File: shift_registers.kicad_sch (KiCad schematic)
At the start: 2 parts

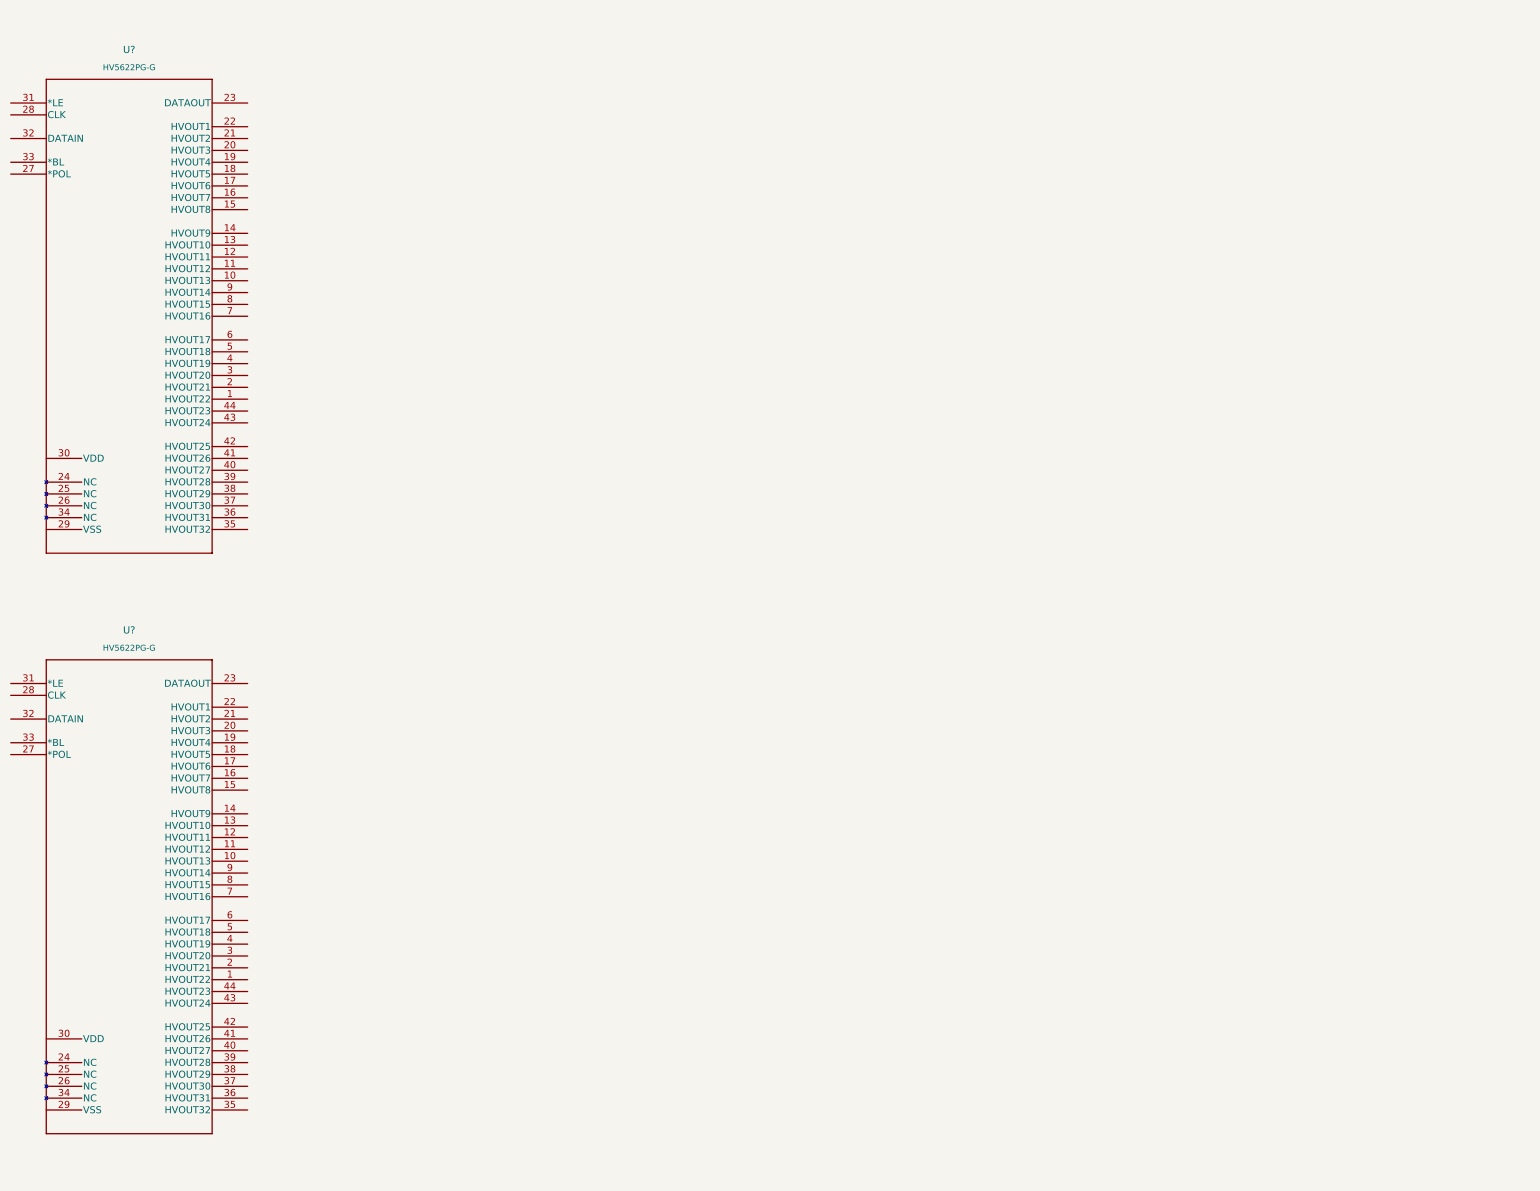
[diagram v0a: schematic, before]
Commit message: added a nixie symbol
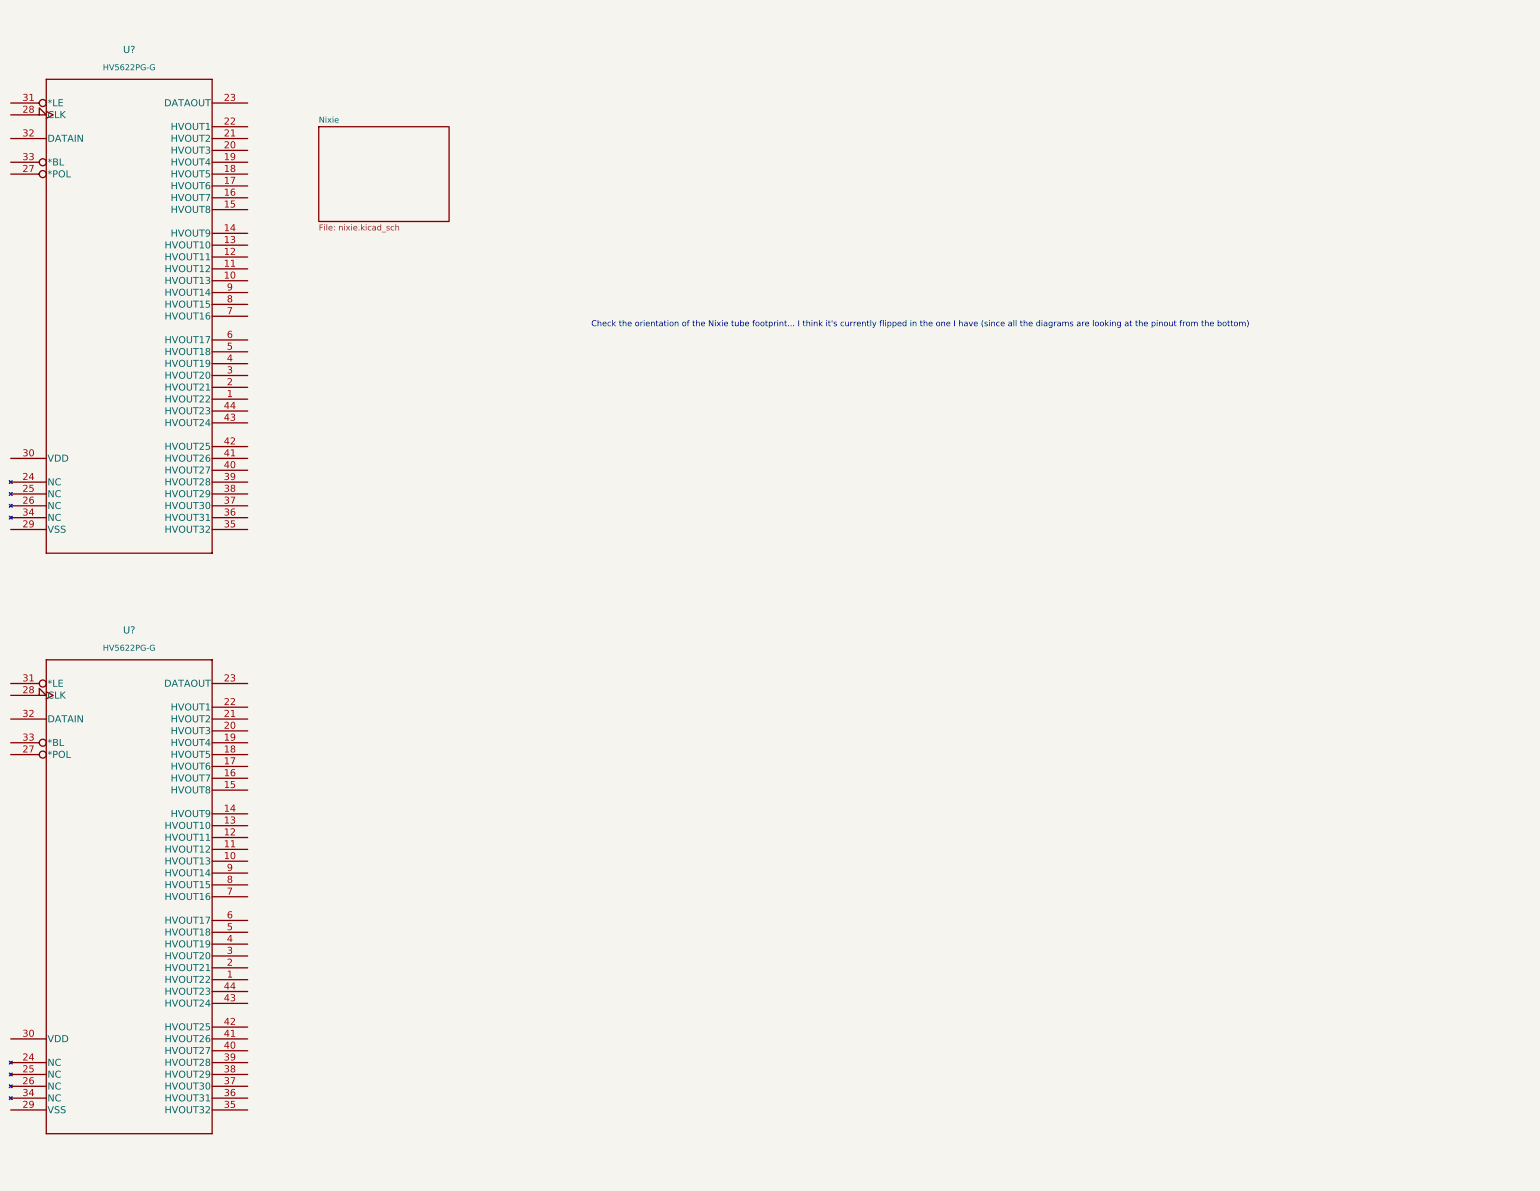
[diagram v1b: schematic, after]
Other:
- added sheet Nixie (nixie.kicad_sch)
- note added: "Check the orientation of the Nixie tube footprint... I think it's currently flipped in the one I have (since all the diagrams are looking at the pinout from the bottom)"
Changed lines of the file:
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@@
 (kicad_sch (version 20211123) (generator eeschema)
   (paper "A3")
-  (symbol (lib_id "arjun_symbols:IC_HV5622PG-G") (at 71.12 162.56 0) (unit 1)
+  (text "Check the orientation of the Nixie tube footprint... I think it's currently flipped in the one I have (since all the diagrams are looking at the pinout from the bottom)"
+    (at 195.58 86.36 0)
+    (effects (font (size 1.27 1.27)) (justify left bottom))
+  )
+  (symbol (lib_name "IC_HV5622PG-G_1") (lib_id "arjun_symbols:IC_HV5622PG-G") (at 71.12 162.56 0) (unit 1)
     (in_bom yes) (on_board yes) (fields_autoplaced)
     (property "Reference" "U?" (id 0) (at 96.52 151.13 0)
@@
     (pin "9")
   )
+  (sheet (at 137.16 43.18) (size 27.94 20.32) (fields_autoplaced)
+    (stroke (width 0.1524) (type solid) (color 0 0 0 0))
+    (fill (color 0 0 0 0.0000))
+    (property "Sheet name" "Nixie" (id 0) (at 137.16 42.4684 0)
+      (effects (font (size 1.27 1.27)) (justify left bottom))
+    )
+    (property "Sheet file" "nixie.kicad_sch" (id 1) (at 137.16 64.0846 0)
+      (effects (font (size 1.27 1.27)) (justify left top))
+    )
+  )
 )

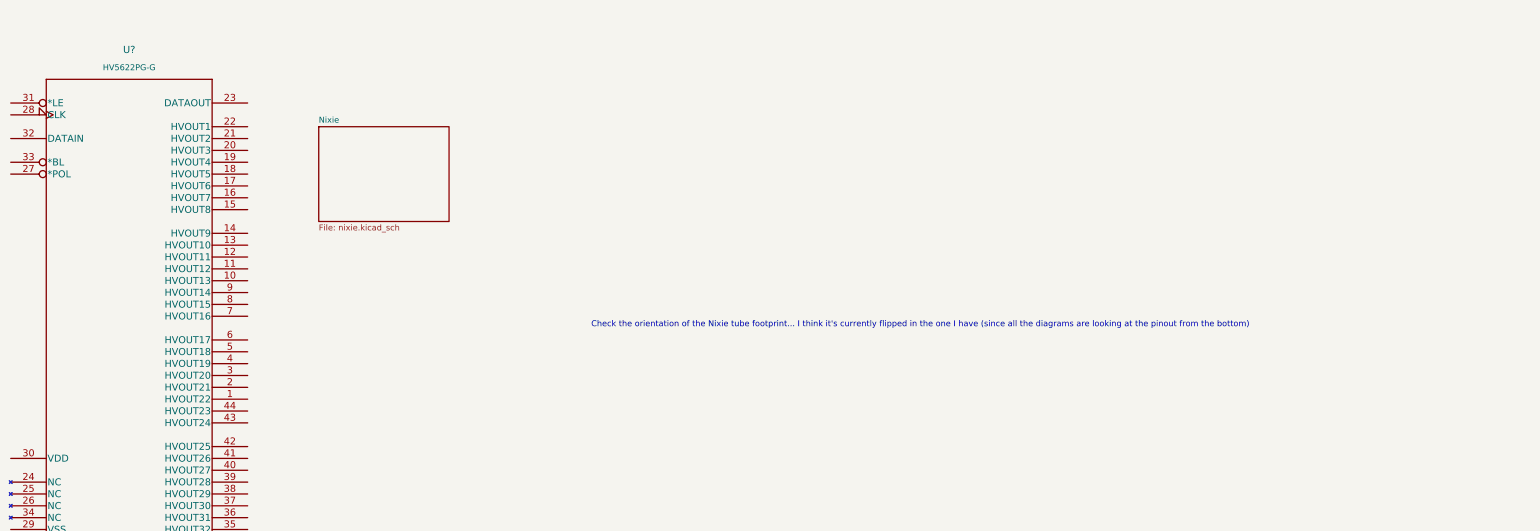
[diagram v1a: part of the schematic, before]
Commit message: updated the nixie schematic
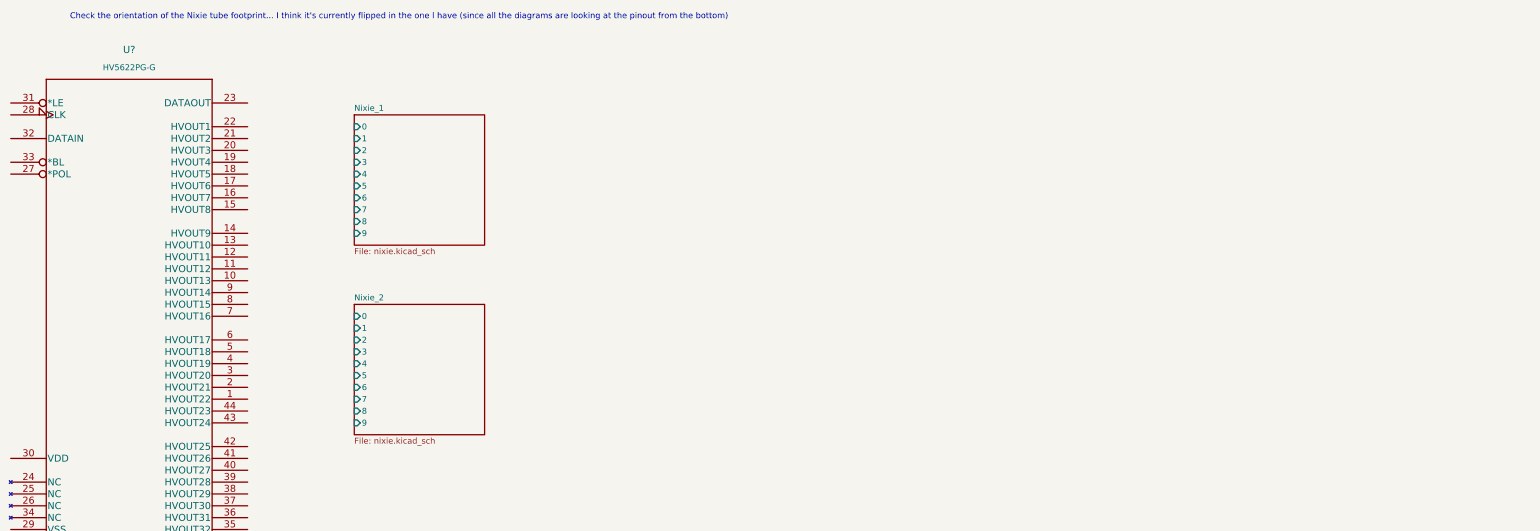
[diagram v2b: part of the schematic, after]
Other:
- sheet Nixie renamed Nixie_1
- added sheet Nixie_2 (nixie.kicad_sch)
- sheet Nixie_1 ports: added 0, 1, 2, 3, 4, 5, 6, 7, 8, 9; removed none
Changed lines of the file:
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@@
   (paper "A3")
   (text "Check the orientation of the Nixie tube footprint... I think it's currently flipped in the one I have (since all the diagrams are looking at the pinout from the bottom)"
-    (at 195.58 86.36 0)
+    (at 83.82 20.32 0)
     (effects (font (size 1.27 1.27)) (justify left bottom))
   )
@@
     (pin "9")
   )
-  (sheet (at 137.16 43.18) (size 27.94 20.32) (fields_autoplaced)
+  (sheet (at 144.78 81.28) (size 27.94 27.94) (fields_autoplaced)
     (stroke (width 0.1524) (type solid) (color 0 0 0 0))
     (fill (color 0 0 0 0.0000))
-    (property "Sheet name" "Nixie" (id 0) (at 137.16 42.4684 0)
+    (property "Sheet name" "Nixie_2" (id 0) (at 144.78 80.5684 0)
       (effects (font (size 1.27 1.27)) (justify left bottom))
     )
-    (property "Sheet file" "nixie.kicad_sch" (id 1) (at 137.16 64.0846 0)
+    (property "Sheet file" "nixie.kicad_sch" (id 1) (at 144.78 109.8046 0)
       (effects (font (size 1.27 1.27)) (justify left top))
     )
-  )
+    (pin "9" input (at 144.78 106.68 180)
+      (effects (font (size 1.27 1.27)) (justify left))
+    )
+    (pin "6" input (at 144.78 99.06 180)
+      (effects (font (size 1.27 1.27)) (justify left))
+    )
+    (pin "8" input (at 144.78 104.14 180)
+      (effects (font (size 1.27 1.27)) (justify left))
+    )
+    (pin "7" input (at 144.78 101.6 180)
+      (effects (font (size 1.27 1.27)) (justify left))
+    )
+    (pin "5" input (at 144.78 96.52 180)
+      (effects (font (size 1.27 1.27)) (justify left))
+    )
+    (pin "1" input (at 144.78 86.36 180)
+      (effects (font (size 1.27 1.27)) (justify left))
+    )
+    (pin "3" input (at 144.78 91.44 180)
+      (effects (font (size 1.27 1.27)) (justify left))
+    )
+    (pin "2" input (at 144.78 88.9 180)
+      (effects (font (size 1.27 1.27)) (justify left))
+    )
+    (pin "0" input (at 144.78 83.82 180)
+      (effects (font (size 1.27 1.27)) (justify left))
+    )
+    (pin "4" input (at 144.78 93.98 180)
+      (effects (font (size 1.27 1.27)) (justify left))
+    )
+  )
+  (sheet (at 144.78 40.64) (size 27.94 27.94) (fields_autoplaced)
+    (stroke (width 0.1524) (type solid) (color 0 0 0 0))
+    (fill (color 0 0 0 0.0000))
+    (property "Sheet name" "Nixie_1" (id 0) (at 144.78 39.9284 0)
+      (effects (font (size 1.27 1.27)) (justify left bottom))
+    )
+    (property "Sheet file" "nixie.kicad_sch" (id 1) (at 144.78 69.1646 0)
+      (effects (font (size 1.27 1.27)) (justify left top))
+    )
+    (pin "9" input (at 144.78 66.04 180)
+      (effects (font (size 1.27 1.27)) (justify left))
+    )
+    (pin "6" input (at 144.78 58.42 180)
+      (effects (font (size 1.27 1.27)) (justify left))
+    )
+    (pin "8" input (at 144.78 63.5 180)
+      (effects (font (size 1.27 1.27)) (justify left))
+    )
+    (pin "7" input (at 144.78 60.96 180)
+      (effects (font (size 1.27 1.27)) (justify left))
+    )
+    (pin "5" input (at 144.78 55.88 180)
+      (effects (font (size 1.27 1.27)) (justify left))
+    )
+    (pin "1" input (at 144.78 45.72 180)
+      (effects (font (size 1.27 1.27)) (justify left))
+    )
+    (pin "3" input (at 144.78 50.8 180)
+      (effects (font (size 1.27 1.27)) (justify left))
+    )
+    (pin "2" input (at 144.78 48.26 180)
+      (effects (font (size 1.27 1.27)) (justify left))
+    )
+    (pin "0" input (at 144.78 43.18 180)
+      (effects (font (size 1.27 1.27)) (justify left))
+    )
+    (pin "4" input (at 144.78 53.34 180)
+      (effects (font (size 1.27 1.27)) (justify left))
+    )
+  )
